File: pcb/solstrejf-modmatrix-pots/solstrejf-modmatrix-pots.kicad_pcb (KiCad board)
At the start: 2 copper layers, 165.7 x 230.5 mm, 56 parts, among them J1 Conn_02x08_Counter_Clockwise, J2 Conn_02x08_Counter_Clockwise, J3 Conn_02x08_Counter_Clockwise, J4 Conn_02x08_Counter_Clockwise

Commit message: updated pcb layout
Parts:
- RV1, RV13, RV25, RV37: value R_Potentiometer -> B10k
- RV10, RV11, RV12, RV14, RV15, RV16, RV17, RV18, RV19, RV2, RV20, RV21, RV22, RV23, RV24, RV26, RV27, RV28, RV29, RV3, RV30, RV31, RV32, RV33, RV34, RV35, RV36, RV38, RV39, RV4, RV40, RV41, RV42, RV43, RV44, RV45, RV46, RV47, RV48, RV5, RV6, RV7, RV8, RV9: value R_Potentiometer -> B10K
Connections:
- J1 pad 10: /V1AMP3 -> /V1FREQ3
- J1 pad 11: /V1AMP2 -> /V1FREQ2
- J1 pad 12: /V1FREQ3 -> /V1AMP3
- J1 pad 13: /V1FREQ2 -> /V1AMP2
- J1 pad 15: /V1FREQ1 -> /V1AMP1
- J1 pad 16: /V1AMP1 -> /V1FREQ1
- J1 pad 4: /V1AMP4 -> /V1FREQ4
- J1 pad 6: /V1FREQ4 -> /V1AMP4
- J2 pad 10: /V2AMP3 -> /V2FREQ3
- J2 pad 11: /V2AMP2 -> /V2FREQ2
- J2 pad 12: /V2FREQ3 -> /V2AMP3
- J2 pad 13: /V2FREQ2 -> /V2AMP2
- J2 pad 15: /V2FREQ1 -> /V2AMP1
- J2 pad 16: /V2AMP1 -> /V2FREQ1
- J2 pad 4: /V2AMP4 -> /V2FREQ4
- J2 pad 6: /V2FREQ4 -> /V2AMP4
- J3 pad 10: /V3AMP3 -> /V3FREQ3
- J3 pad 11: /V3AMP2 -> /V3FREQ2
- J3 pad 12: /V3FREQ3 -> /V3AMP3
- J3 pad 13: /V3FREQ2 -> /V3AMP2
- J3 pad 15: /V3FREQ1 -> /V3AMP1
- J3 pad 16: /V3AMP1 -> /V3FREQ1
- J3 pad 4: /V3AMP4 -> /V3FREQ4
- J3 pad 6: /V3FREQ4 -> /V3AMP4
- J4 pad 10: /V4AMP3 -> /V4FREQ3
- J4 pad 11: /V4AMP2 -> /V4FREQ2
- J4 pad 12: /V4FREQ3 -> /V4AMP3
- J4 pad 13: /V4FREQ2 -> /V4AMP2
- J4 pad 15: /V4FREQ1 -> /V4AMP1
- J4 pad 16: /V4AMP1 -> /V4FREQ1
- J4 pad 4: /V4AMP4 -> /V4FREQ4
- J4 pad 6: /V4FREQ4 -> /V4AMP4
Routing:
- net /VOICE1: track 0.00 -> 387.1 mm
- net /VOICE2: track 0.00 -> 333.3 mm
- net /VOICE3: track 0.00 -> 279.4 mm
- net /VOICE4: track 0.00 -> 230.5 mm
- net /V2PAN1: track 0.00 -> 226.4 mm
- net /V1PAN1: track 0.00 -> 225.8 mm
- net /V1FREQ1: track 0.00 -> 222.1 mm
- net /V2FREQ1: track 0.00 -> 221.9 mm
- net /V2AMP1: track 0.00 -> 221.1 mm
- net /V1AMP1: track 0.00 -> 220.4 mm
- net /V2PAN2: track 0.00 -> 176.8 mm, vias 0 -> 1
- net /V1PAN2: track 0.00 -> 176.5 mm, vias 0 -> 1
- net /V1FREQ2: track 0.00 -> 172.2 mm, vias 0 -> 1
- net /V2FREQ2: track 0.00 -> 171.7 mm, vias 0 -> 1
- net /V1AMP2: track 0.00 -> 167.6 mm, vias 0 -> 1
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
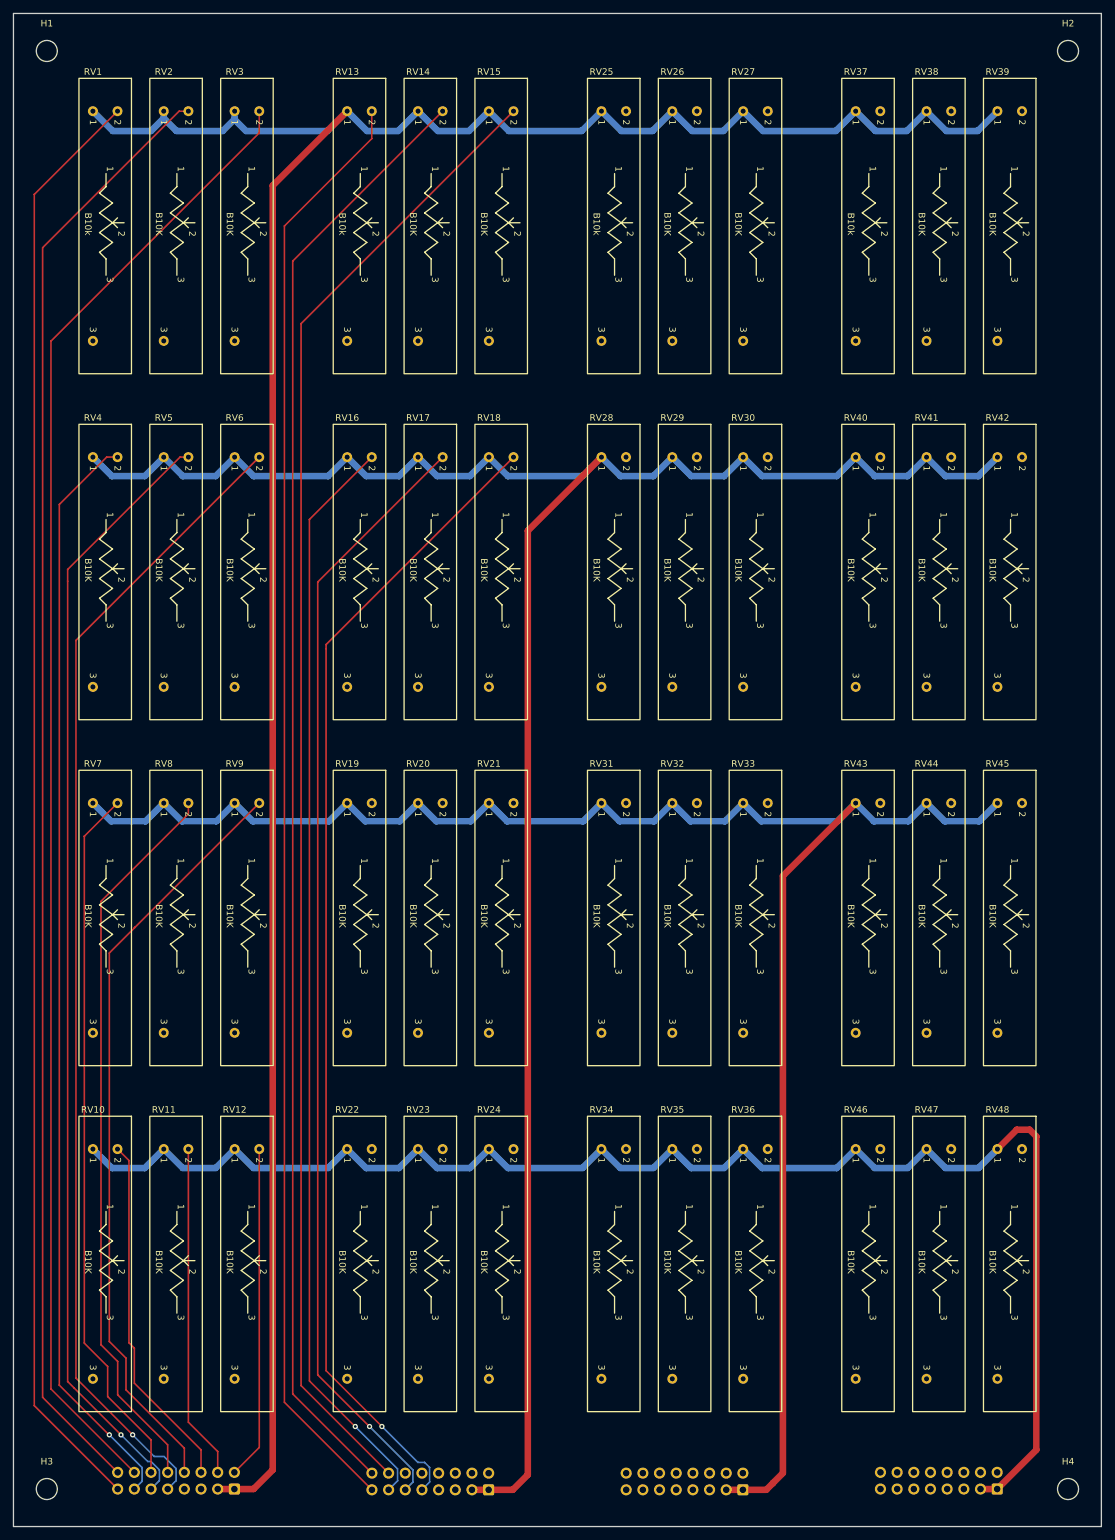
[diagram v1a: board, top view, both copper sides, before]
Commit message: Finished routing of modmatrix!
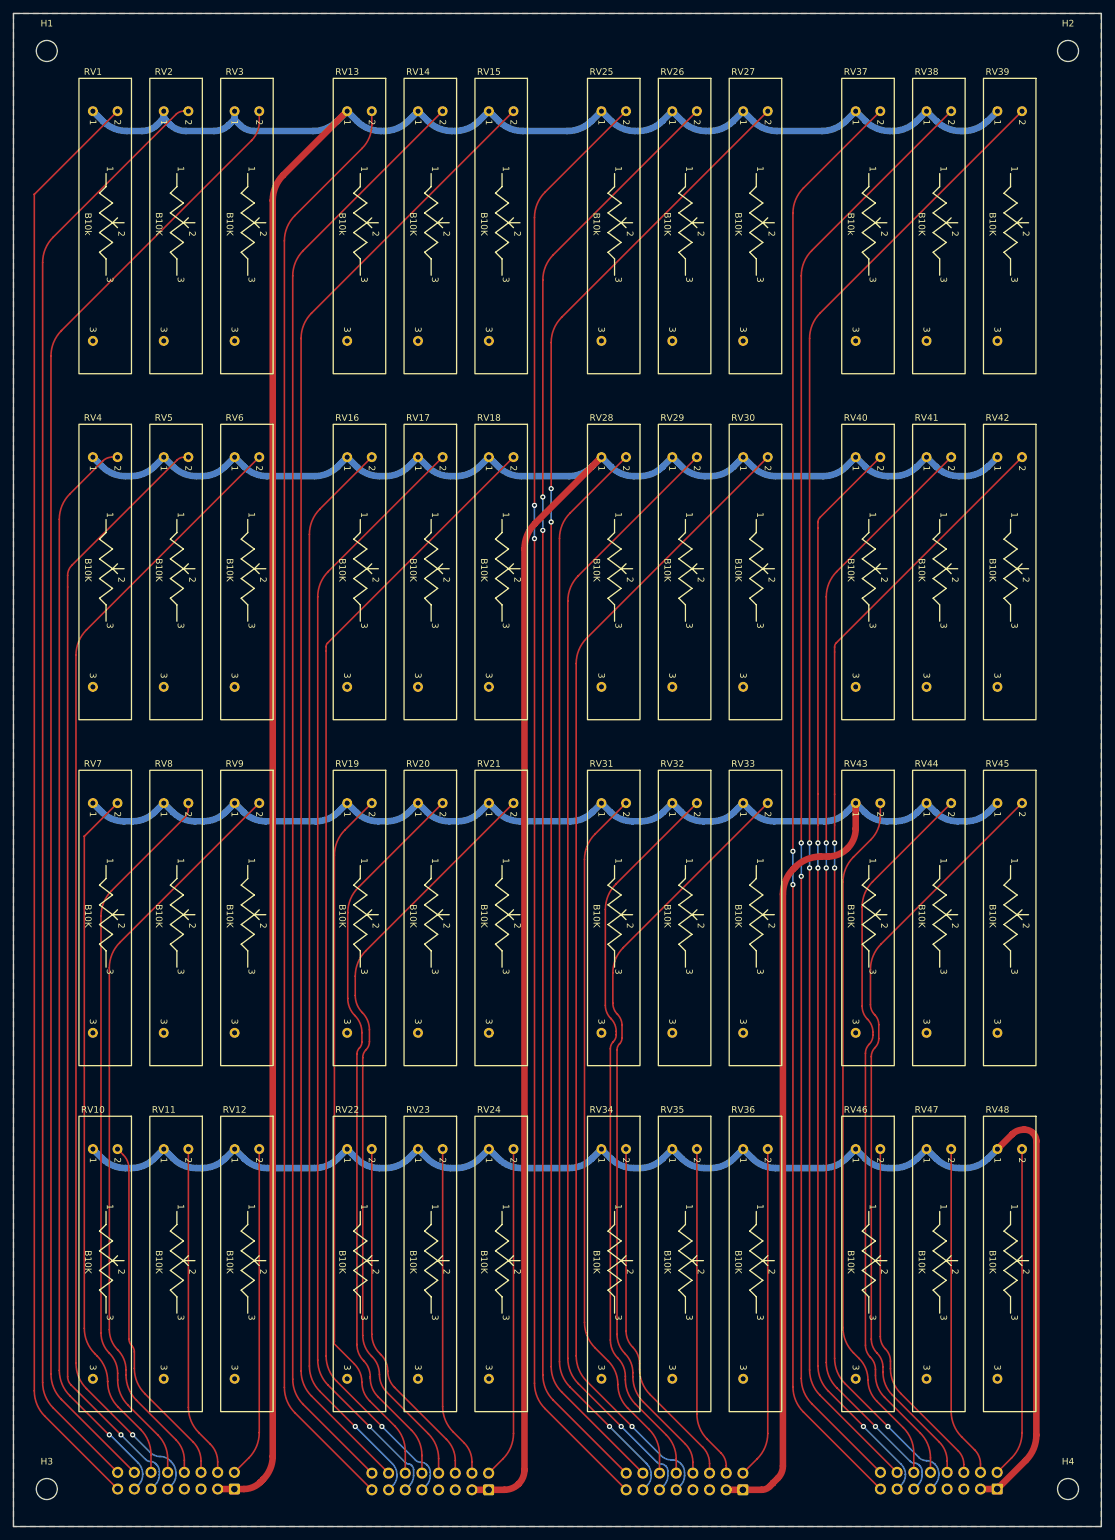
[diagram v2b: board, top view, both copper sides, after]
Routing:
- net /V3PAN1: track 0.00 -> 226.6 mm, vias 0 -> 2
- net /V4PAN1: track 0.00 -> 225.8 mm, vias 0 -> 2
- net /V3FREQ1: track 0.00 -> 222.1 mm, vias 0 -> 2
- net /V4FREQ1: track 0.00 -> 221.3 mm, vias 0 -> 2
- net /V3AMP1: track 0.00 -> 221.1 mm, vias 0 -> 2
- net /V4AMP1: track 0.00 -> 220.4 mm, vias 0 -> 2
- net /V3PAN2: track 0.00 -> 176.9 mm, vias 0 -> 1
- net /V4PAN2: track 0.00 -> 176.4 mm, vias 0 -> 3
- net /V3FREQ2: track 0.00 -> 172.0 mm, vias 0 -> 1
- net /V4FREQ2: track 0.00 -> 171.5 mm, vias 0 -> 3
- net /V3AMP2: track 0.00 -> 167.1 mm, vias 0 -> 1
- net /V4AMP2: track 0.00 -> 166.8 mm, vias 0 -> 3
- net /V2PAN3: track 0.00 -> 116.5 mm
- net /V3PAN3: track 0.00 -> 116.1 mm
- net /V4PAN3: track 0.00 -> 115.9 mm
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- added copper zone on B.Cu, net GND
- added copper zone on F.Cu, net GND

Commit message: updated .gitignore. Added silkscreen text to pcb.
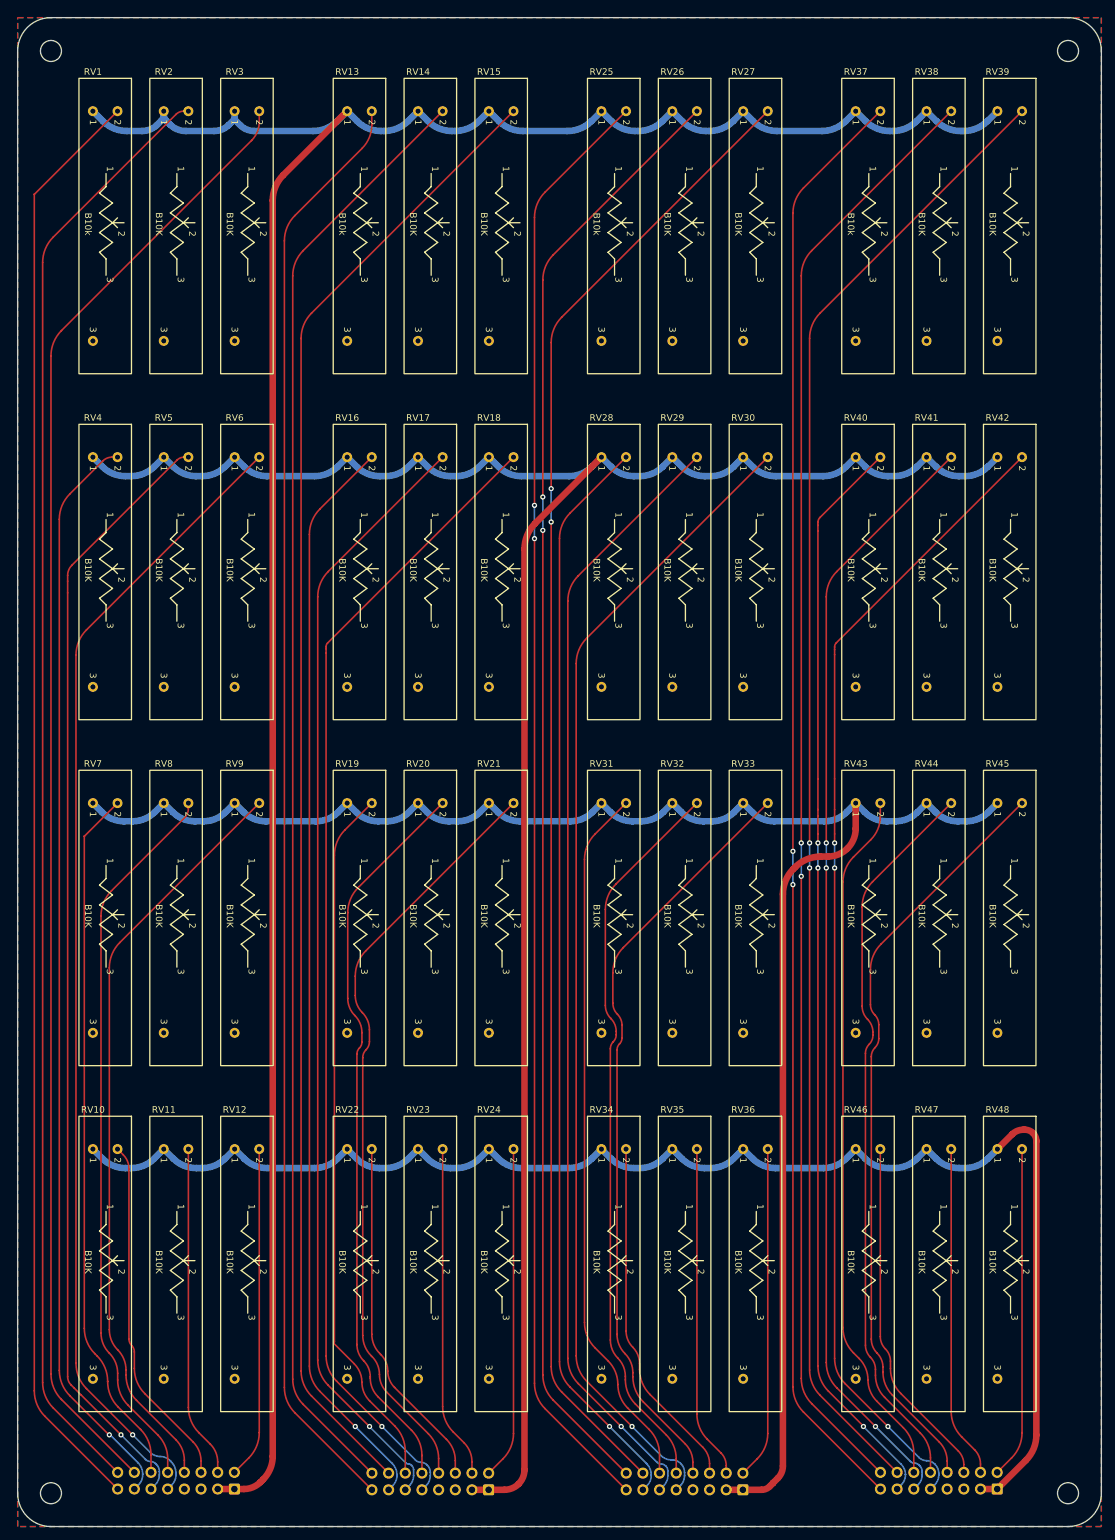
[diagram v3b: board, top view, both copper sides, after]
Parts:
- moved H3 0.90 mm to (-10.2, 236.2)
- moved H1 0.63 mm to (-10.2, 16.5)
- moved H4 0.63 mm to (144.8, 236.2)
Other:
- board size 165.7 x 230.5 mm -> 165.1 x 229.9 mm
- board text added: "Kromftronics // Solfstrejf ModMatrix RevA"
- board text added: "Voice 1 Connection"
- board text added: "Voice 2 Connection"
- board text added: "Voice 3 Connection"
- board text added: "Voice 4 Connection"

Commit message: Added kromftronics custom kicad files as submodule. Updated modmatrix KiCad project to use the submodule.
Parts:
- RV1, RV10, RV11, RV12, RV13, RV14, RV15, RV16, RV17, RV18, RV19, RV2, RV20, RV21, RV22, RV23, RV24, RV25, RV26, RV27, RV28, RV29, RV3, RV30, RV31, RV32, RV33, RV34, RV35, RV36, RV37, RV38, RV39, RV4, RV40, RV41, RV42, RV43, RV44, RV45, RV46, RV47, RV48, RV5, RV6, RV7, RV8, RV9: footprint Kromtronics_Custom:Potentiometer_Alpha_slide_pot_30mm -> Kromftronics_Custom:Potentiometer_Alpha_slide_pot_30mm
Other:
- board text added: "Kromftronics // Solfstrejf ModMatrix Rev1"
- board text removed: "Kromftronics // Solfstrejf ModMatrix RevA"

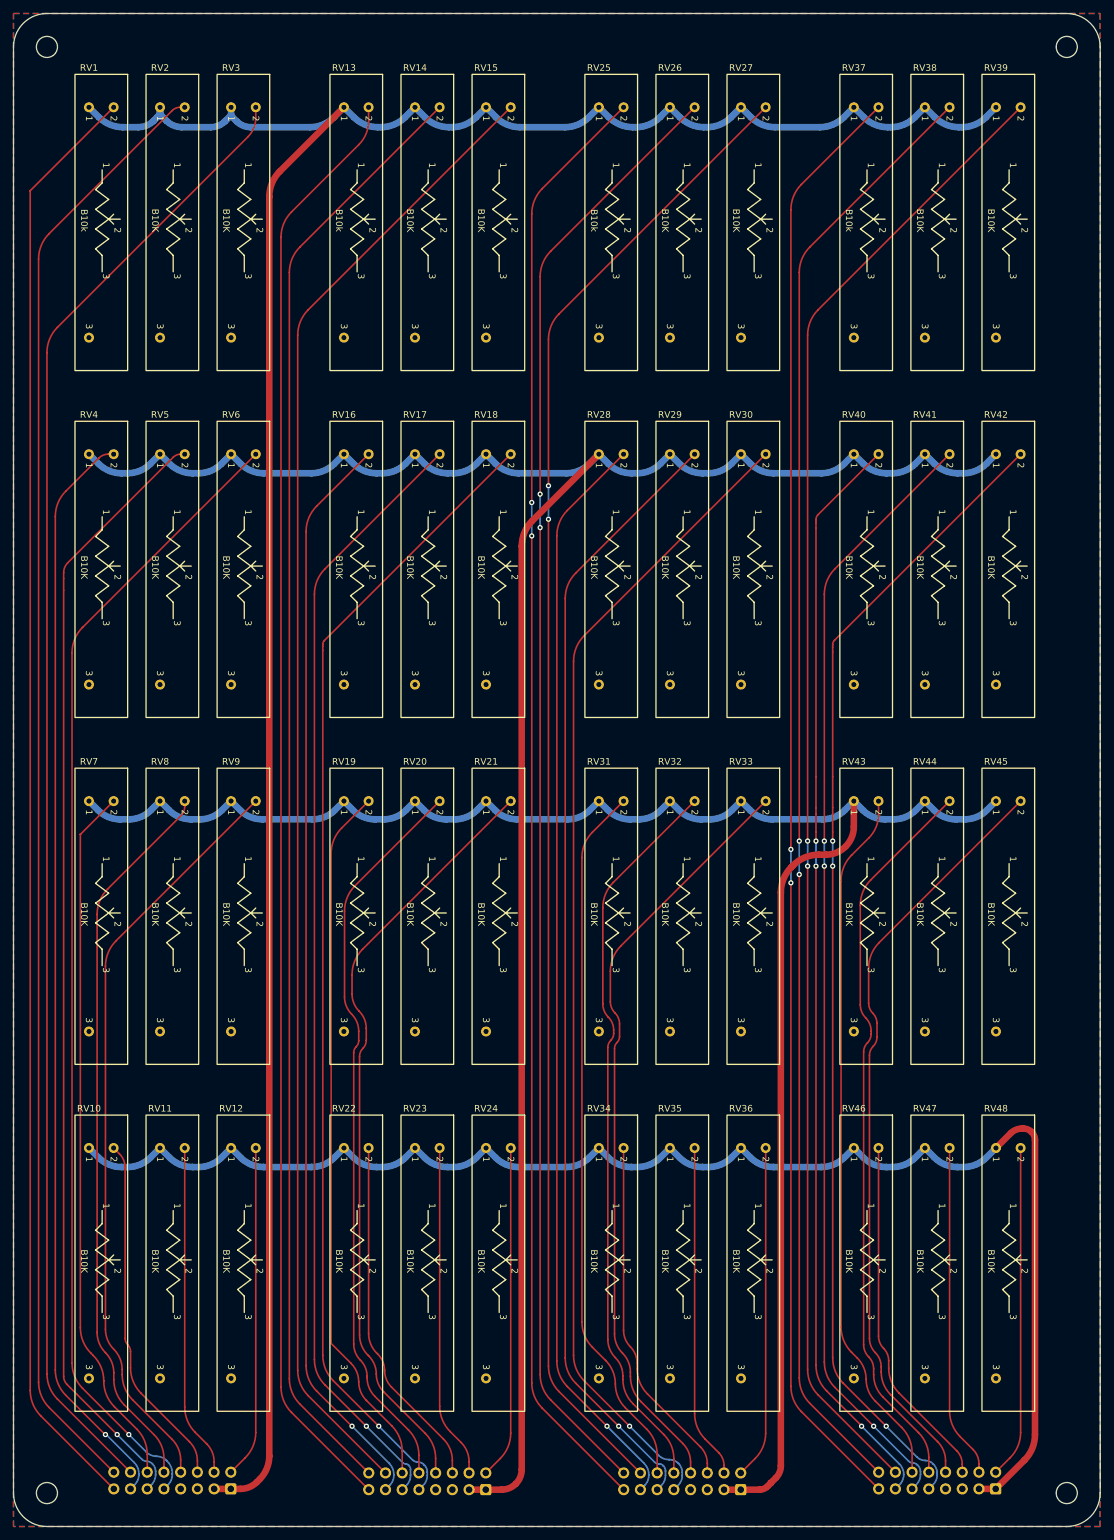
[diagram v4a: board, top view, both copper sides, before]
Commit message: Updated modmatrix project: added more silkscreen and removed rounded edges. Stored 3D models in mod-matrix project for better portability. Added new images of the current state of the mod-matrix PCB.
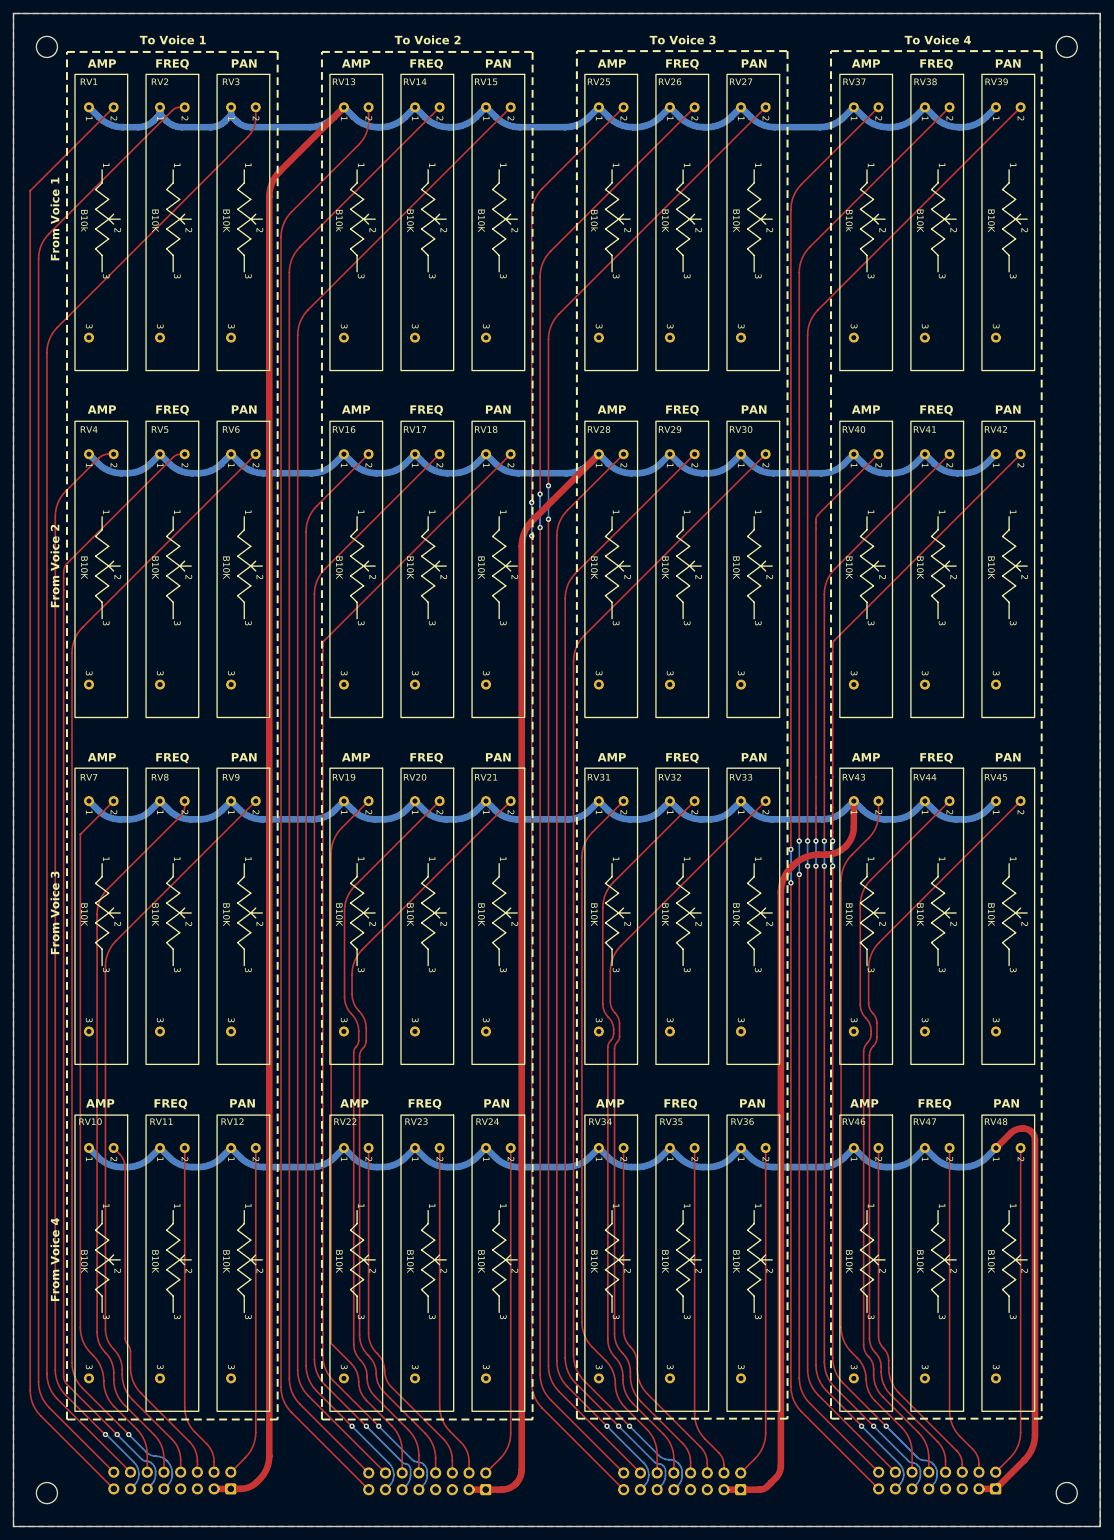
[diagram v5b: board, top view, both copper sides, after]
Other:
- outline, holes or cut-outs redrawn
- board text added: "AMP"
- board text added: "FREQ"
- board text added: "From Voice 1"
- board text added: "From Voice 2"
- board text added: "From Voice 3"
- board text added: "From Voice 4"
- board text added: "Kromftronics // Solfstrejf ModMatrix Rev 1.0"
- board text added: "PAN"
- board text added: "To Voice 1"
- board text added: "To Voice 2"
- board text added: "To Voice 3"
- board text added: "To Voice 4"
- board text removed: "Kromftronics // Solfstrejf ModMatrix Rev1"
